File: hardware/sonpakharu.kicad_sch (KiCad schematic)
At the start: 28 parts, among them IC1 ESP32-S3-WROOM-1U-N4, J1 FTDI, Q1 DMG2301L, Q2 S8050, Q3 S8050, SW1 Reset, SW2 Reset, U1 AP2112K-3.3TRG1, U2 MCP73831-2-OT

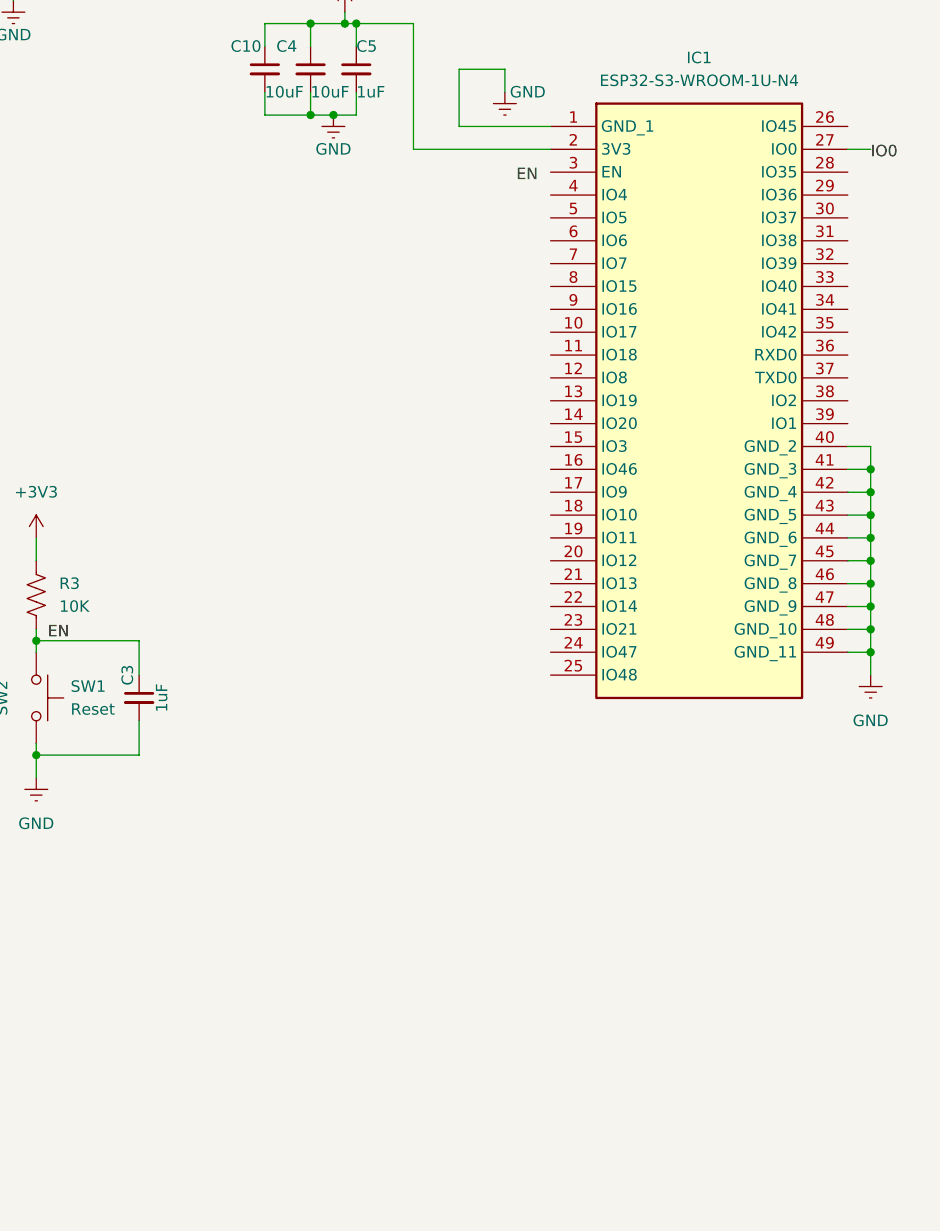
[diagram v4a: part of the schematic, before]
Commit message: added adc
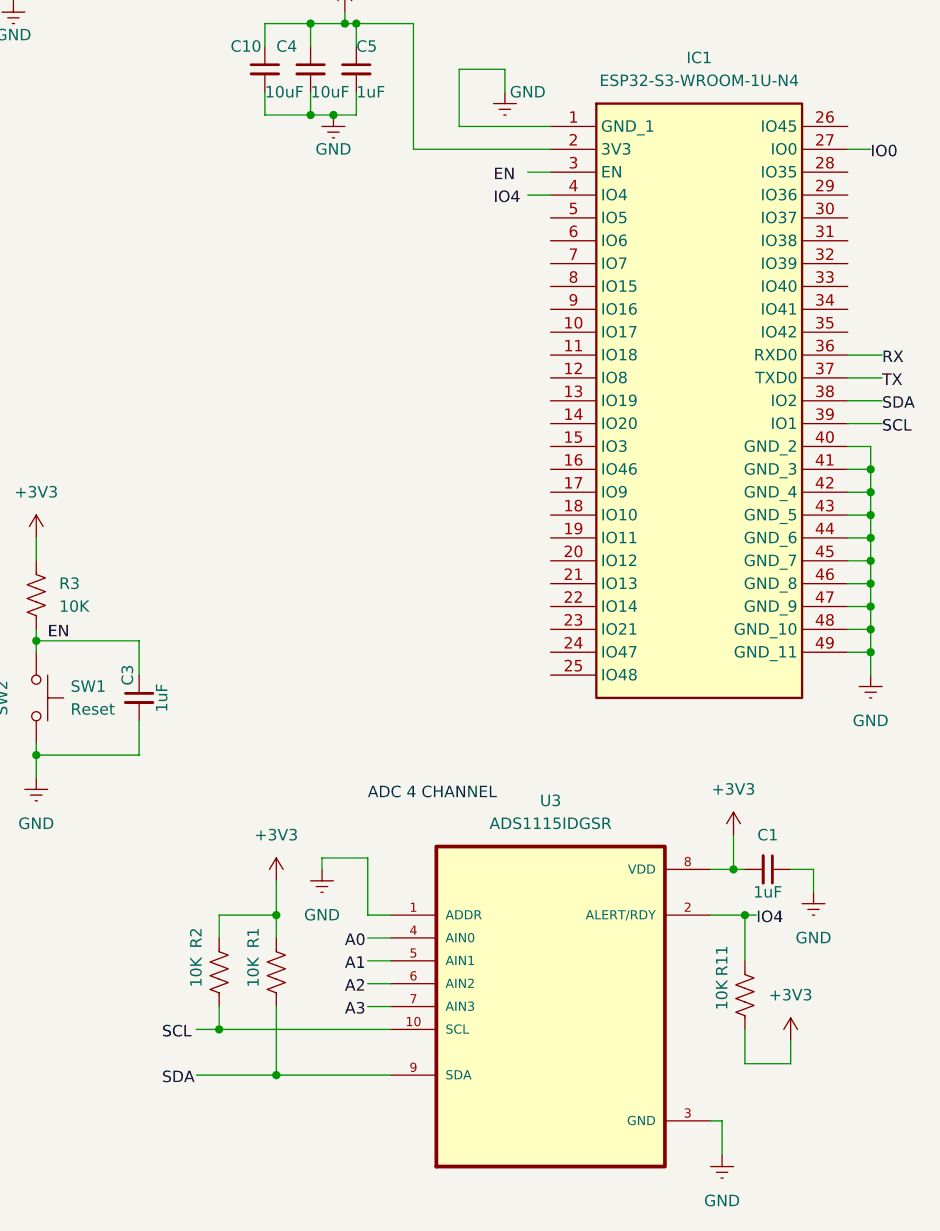
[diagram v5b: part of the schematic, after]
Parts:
- added C1: 1uF, symbol Device:C_Small
- added R1, R11, R2: 10K, symbol Device:R_US
- added U3: ADS1115IDGSR, ADS1115IDGSR:SOP50P490X110-10N, symbol ADS1115IDGSR:ADS1115IDGSR
- IC1: MPN (none) -> C3013945
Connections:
- net +3V3: now also C1.2, R1.1, R11.2, R2.1, U3.8 (VDD)
- net GND: now also C1.1, U3.1 (ADDR), U3.3 (GND)
- new net: R2.2, U3.10 (SCL)
- new net: R1.2, U3.9 (SDA)
- new net: R11.1, U3.2 (ALERT/RDY)
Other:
- note added: "ADC 4 CHANNEL"

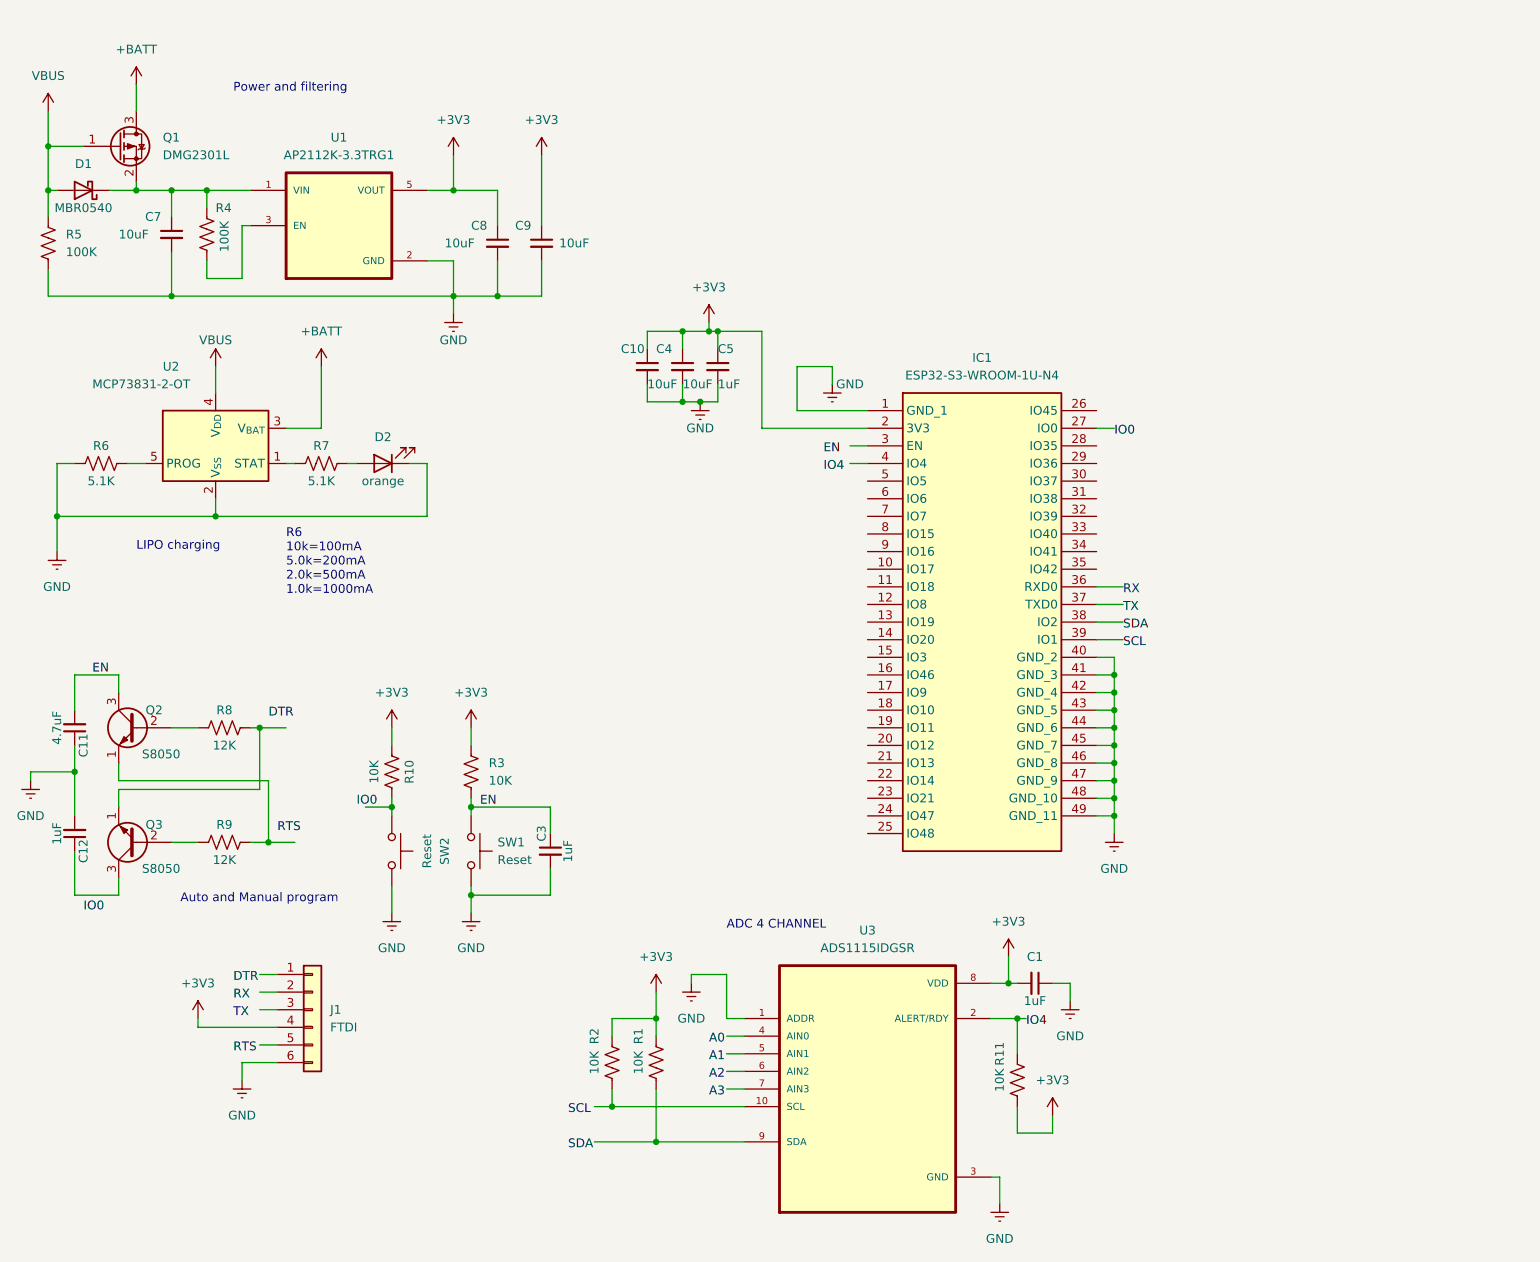
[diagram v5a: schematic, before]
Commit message: added gpio connectors
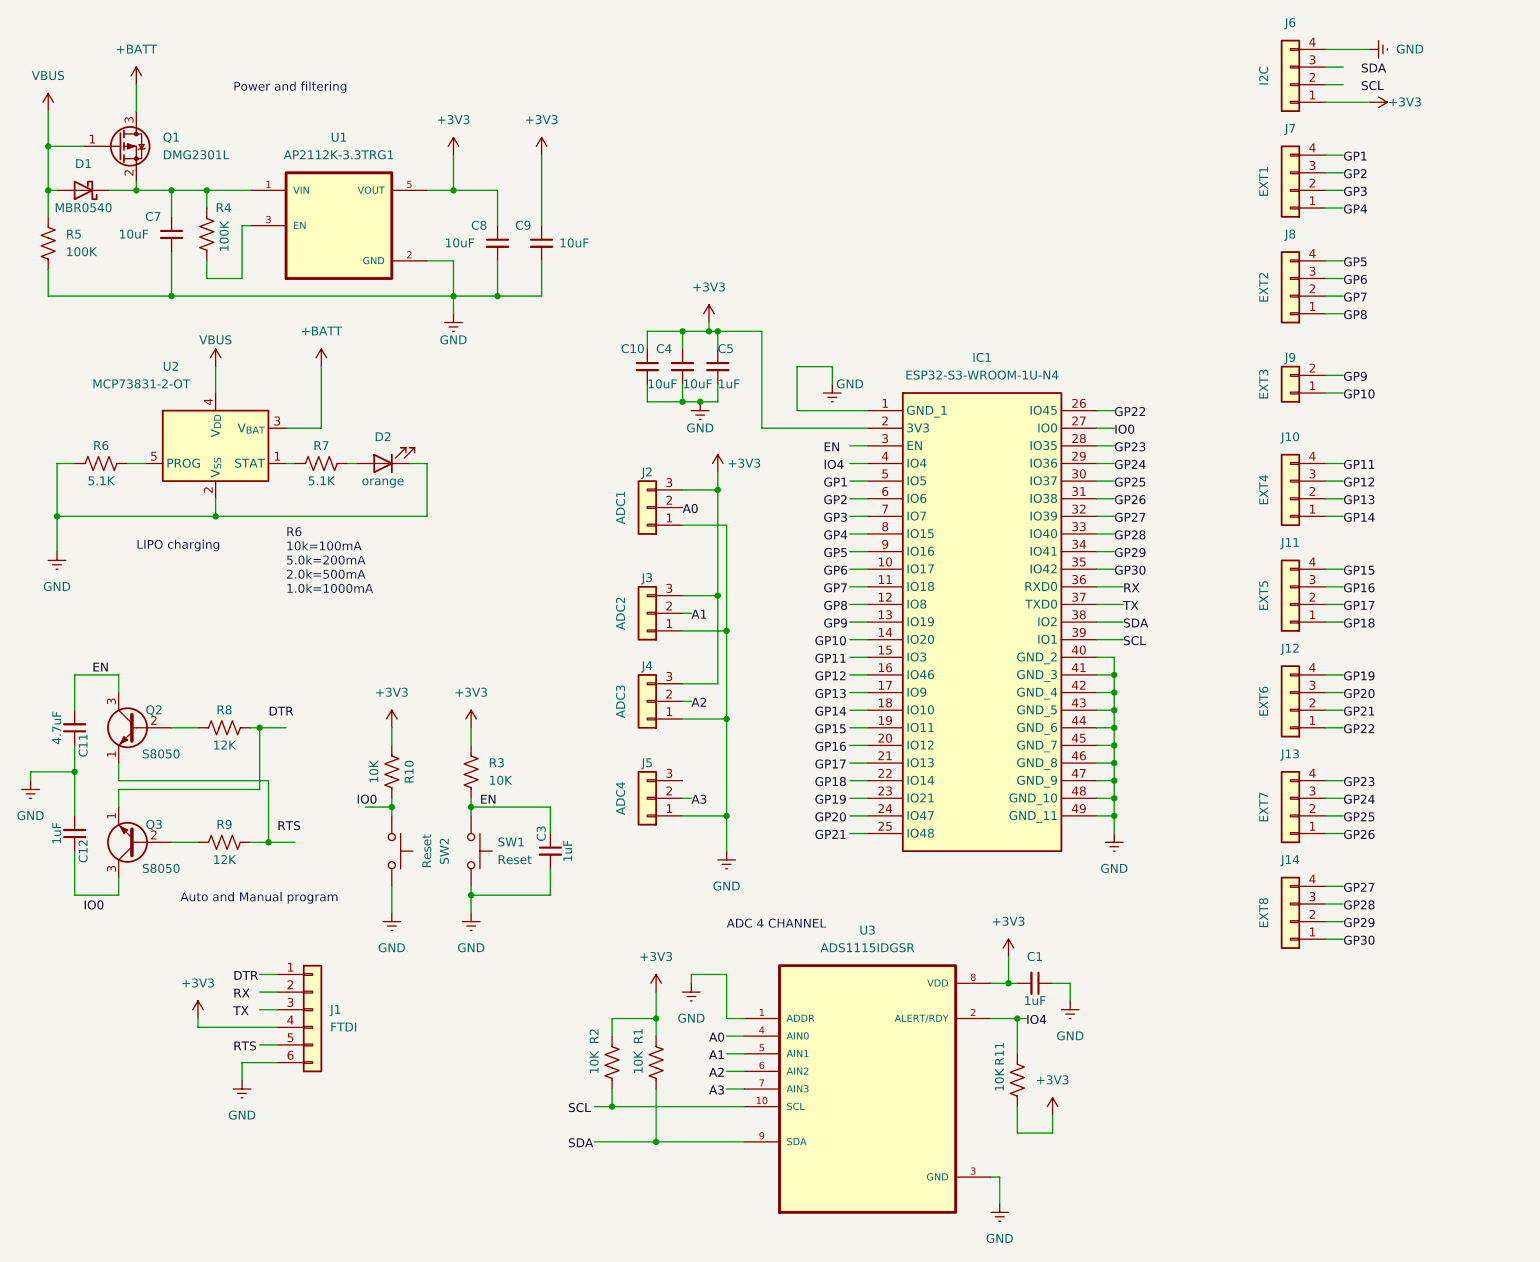
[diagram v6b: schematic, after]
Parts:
- added J10: EXT4, symbol Connector_Generic:Conn_01x04
- added J11: EXT5, symbol Connector_Generic:Conn_01x04
- added J12: EXT6, symbol Connector_Generic:Conn_01x04
- added J13: EXT7, symbol Connector_Generic:Conn_01x04
- added J14: EXT8, symbol Connector_Generic:Conn_01x04
- added J2: ADC1, symbol Connector_Generic:Conn_01x03
- added J3: ADC2, symbol Connector_Generic:Conn_01x03
- added J4: ADC3, symbol Connector_Generic:Conn_01x03
- added J5: ADC4, symbol Connector_Generic:Conn_01x03
- added J6: I2C, symbol Connector_Generic:Conn_01x04
- added J7: EXT1, symbol Connector_Generic:Conn_01x04
- added J8: EXT2, symbol Connector_Generic:Conn_01x04
- added J9: EXT3, symbol Connector_Generic:Conn_01x02
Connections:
- net +3V3: now also J2.3 (Pin_3), J3.3 (Pin_3), J4.3 (Pin_3), J6.1 (Pin_1)
- net GND: now also J2.1 (Pin_1), J3.1 (Pin_1), J4.1 (Pin_1), J5.1 (Pin_1), J6.4 (Pin_4)

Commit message: added battery connector
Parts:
- added J15: BATTERY, symbol Connector_Generic:Conn_01x02
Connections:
- net +BATT: now also J15.2 (Pin_2)
- net GND: now also J15.1 (Pin_1)
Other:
- moved on the sheet: C10, C4, C5, IC1, J2, J3, J4, J5

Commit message: main power
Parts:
- added J16: PWR, symbol Connector_Generic:Conn_01x02
- J15: value BATTERY -> BATT
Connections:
- net GND: now also J16.1 (Pin_1)
- net VBUS: now also J16.2 (Pin_2)
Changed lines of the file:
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@@
     (stroke (width 0) (type default))
   )
+  (wire (pts (xy 226.06 101.6) (xy 228.6 101.6))
+    (stroke (width 0) (type default))
+  )
   (wire (pts (xy 172.72 105.41) (xy 175.26 105.41))
     (stroke (width 0) (type default))
@@
     (stroke (width 0) (type default))
   )
+  (wire (pts (xy 226.06 99.06) (xy 228.6 99.06))
+    (stroke (width 0) (type default))
+  )
   (wire (pts (xy 46.99 55.88) (xy 46.99 48.26))
     (stroke (width 0) (type default))
@@
     (stroke (width 0) (type default))
   )
+  (wire (pts (xy 228.6 99.06) (xy 228.6 96.52))
+    (stroke (width 0) (type default))
+  )
   (wire (pts (xy 19.05 36.83) (xy 19.05 43.18))
     (stroke (width 0) (type default))
@@
     (stroke (width 0) (type default))
   )
+  (wire (pts (xy 228.6 101.6) (xy 228.6 104.14))
+    (stroke (width 0) (type default))
+  )
   (wire (pts (xy 29.21 142.24) (xy 29.21 144.78))
     (stroke (width 0) (type default))
@@
     )
   )
+  (symbol (lib_id "LoRa_PCIe_GW-rescue:GND") (at 228.6 104.14 0) (unit 1)
+    (in_bom yes) (on_board yes) (dnp no) (fields_autoplaced)
+    (property "Reference" "#PWR033" (at 228.6 100.965 0)
+      (effects (font (size 1.27 1.27)) hide)
+    )
+    (property "Value" "GND" (at 228.6 109.22 0)
+      (effects (font (size 1.27 1.27)))
+    )
+    (property "Footprint" "" (at 223.52 104.14 0)
+      (effects (font (size 1.27 1.27)) hide)
+    )
+    (property "Datasheet" "" (at 223.52 104.14 0)
+      (effects (font (size 1.27 1.27)) hide)
+    )
+    (pin "1")
+    (instances
+      (project "sonpakharu"
+        (path "/7446772e-77ef-4971-88a7-8e2cc94b8894"
+          (reference "#PWR033") (unit 1)
+        )
+      )
+    )
+  )
   (symbol (lib_id "Device:R_US") (at 80.01 127 180) (unit 1)
     (in_bom yes) (on_board yes) (dnp no) (fields_autoplaced)
@@
       (effects (font (size 1.27 1.27)))
     )
-    (property "Value" "BATTERY" (at 217.17 71.12 90)
+    (property "Value" "BATT" (at 217.17 71.12 90)
       (effects (font (size 1.27 1.27)))
     )
@@
     )
   )
+  (symbol (lib_id "power:VBUS") (at 228.6 96.52 0) (unit 1)
+    (in_bom yes) (on_board yes) (dnp no) (fields_autoplaced)
+    (property "Reference" "#PWR032" (at 228.6 100.33 0)
+      (effects (font (size 1.27 1.27)) hide)
+    )
+    (property "Value" "VBUS" (at 228.6 91.44 0)
+      (effects (font (size 1.27 1.27)))
+    )
+    (property "Footprint" "" (at 228.6 96.52 0)
+      (effects (font (size 1.27 1.27)) hide)
+    )
+    (property "Datasheet" "" (at 228.6 96.52 0)
+      (effects (font (size 1.27 1.27)) hide)
+    )
+    (pin "1")
+    (instances
+      (project "sonpakharu"
+        (path "/7446772e-77ef-4971-88a7-8e2cc94b8894"
+          (reference "#PWR032") (unit 1)
+        )
+      )
+    )
+  )
   (symbol (lib_id "LoRa_PCIe_GW-rescue:GND") (at 20.32 95.25 0) (unit 1)
     (in_bom yes) (on_board yes) (dnp no) (fields_autoplaced)
@@
         )
       )
+    )
+  )
+  (symbol (lib_id "Connector_Generic:Conn_01x02") (at 220.98 101.6 180) (unit 1)
+    (in_bom yes) (on_board yes) (dnp no)
+    (property "Reference" "J16" (at 220.98 96.52 0)
+      (effects (font (size 1.27 1.27)))
+    )
+    (property "Value" "PWR" (at 217.17 100.33 90)
+      (effects (font (size 1.27 1.27)))
+    )
+    (property "Footprint" "" (at 220.98 101.6 0)
+      (effects (font (size 1.27 1.27)) hide)
+    )
+    (property "Datasheet" "~" (at 220.98 101.6 0)
+      (effects (font (size 1.27 1.27)) hide)
+    )
+    (pin "1")
+    (pin "2")
+    (instances
+      (project "sonpakharu"
+        (path "/7446772e-77ef-4971-88a7-8e2cc94b8894"
+          (reference "J16") (unit 1)
+        )
+      )
